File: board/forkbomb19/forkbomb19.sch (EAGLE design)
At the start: 65 parts, among them SW1 SPST_TACT-KMR2, T3 MMUN2133LT1G, U1 ESP-WROOM-03, U4 TPS61090RSAR, U5 MCP73871, X3 POT_GND, X4 POT_3V3, X5 POT_SIG

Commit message: small cleanup
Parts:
- removed HRDRST: JUMPER-SMT_2_NO_SILK_ROUND, SparkFun-Jumpers:JUMPER-SMT_2_NO_SILK_ROUND
- added SW2: SPST_TACT-KMR2, adafruit:SPST_TACT-KMR2
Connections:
- net EN: now also SW2.S, SW2.S1; no longer HRDRST.2
- net GND: now also SW2.P, SW2.P1; no longer HRDRST.1
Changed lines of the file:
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@@
 <parts>
 <part name="U1" library="forkbomb19" deviceset="ESP-WROOM-03" device=""/>
-<part name="HRDRST" library="SparkFun-Jumpers" library_urn="urn:adsk.eagle:library:528" deviceset="JUMPER-SMT_2_NO" device="_SILK_ROUND" package3d_urn="urn:adsk.eagle:package:39280/1" value=""/>
 <part name="R1" library="resistor" library_urn="urn:adsk.eagle:library:348" deviceset="R-US_" device="R0603" package3d_urn="urn:adsk.eagle:package:23555/2" value="1k"/>
 <part name="C1" library="resistor" library_urn="urn:adsk.eagle:library:348" deviceset="C-US" device="C0603" package3d_urn="urn:adsk.eagle:package:23616/2" value="100nF"/>
@@
 <part name="U$20" library="microbuilder" deviceset="GND" device=""/>
 <part name="U$23" library="microbuilder" deviceset="VBAT" device=""/>
-<part name="T3" library="transistor" deviceset="*-PNP_DRIVER-" device="SC59-BEC" technology="MUN2114T1" value="MMUN2133LT1G"/>
+<part name="T3" library="transistor" library_urn="urn:adsk.eagle:library:402" deviceset="*-PNP_DRIVER-" device="SC59-BEC" package3d_urn="urn:adsk.eagle:package:28754/2" technology="MUN2114T1" value="MMUN2133LT1G"/>
 <part name="GND22" library="supply1" deviceset="GND" device=""/>
 <part name="R25" library="rcl" library_urn="urn:adsk.eagle:library:334" deviceset="R-US_" device="R0603" package3d_urn="urn:adsk.eagle:package:23555/2" value="270K"/>
@@
 <part name="+3V16" library="supply1" library_urn="urn:adsk.eagle:library:371" deviceset="+3V3" device=""/>
 <part name="U$8" library="forkbomb19" deviceset="JS202011JAQN" device=""/>
+<part name="SW2" library="adafruit" library_urn="urn:adsk.eagle:library:420" deviceset="SPST_TACT" device="-KMR2" package3d_urn="urn:adsk.eagle:package:6240885/1"/>
 </parts>
 <sheets>
@@
 <attribute name="VALUE" x="-15.24" y="-38.354" size="1.778" layer="96" align="top-left"/>
 </instance>
-<instance part="HRDRST" gate="G$1" x="-35.56" y="30.48" smashed="yes">
-<attribute name="NAME" x="-38.1" y="33.02" size="1.778" layer="95" font="vector"/>
-<attribute name="VALUE" x="-38.1" y="27.94" size="1.778" layer="96" font="vector" align="top-left"/>
-</instance>
 <instance part="R1" gate="G$1" x="-25.4" y="35.56" smashed="yes" rot="R90">
 <attribute name="NAME" x="-26.8986" y="31.75" size="1.778" layer="95" rot="R90"/>
@@
 <attribute name="VALUE" x="-20.32" y="45.72" size="1.778" layer="96" rot="R90"/>
 </instance>
-<instance part="GND2" gate="1" x="-43.18" y="25.4" smashed="yes">
-<attribute name="VALUE" x="-45.72" y="22.86" size="1.778" layer="96"/>
+<instance part="GND2" gate="1" x="-48.26" y="25.4" smashed="yes">
+<attribute name="VALUE" x="-50.8" y="22.86" size="1.778" layer="96"/>
 </instance>
 <instance part="GND3" gate="1" x="-2.54" y="40.64" smashed="yes">
@@
 </instance>
 <instance part="+3V2" gate="G$1" x="66.04" y="-25.4" smashed="yes">
-<attribute name="VALUE" x="63.5" y="-30.48" size="1.778" layer="96" rot="R90"/>
+<attribute name="VALUE" x="68.58" y="-25.4" size="1.778" layer="96"/>
 </instance>
 <instance part="C3" gate="G$1" x="25.4" y="48.26" smashed="yes">
@@
 </instance>
 <instance part="X3" gate="-1" x="66.04" y="-44.45" smashed="yes" rot="R90">
-<attribute name="VALUE" x="64.77" y="-45.72" size="1.778" layer="96" rot="R90"/>
-<attribute name="NAME" x="66.802" y="-41.91" size="1.524" layer="95" rot="R90"/>
+<attribute name="VALUE" x="63.5" y="-57.15" size="1.778" layer="96"/>
+<attribute name="NAME" x="72.39" y="-54.102" size="1.524" layer="95"/>
 </instance>
 <instance part="X4" gate="-1" x="66.04" y="-31.75" smashed="yes" rot="R270">
-<attribute name="VALUE" x="67.31" y="-30.48" size="1.778" layer="96" rot="R270"/>
-<attribute name="NAME" x="65.278" y="-34.29" size="1.524" layer="95" rot="R270"/>
+<attribute name="VALUE" x="68.58" y="-29.21" size="1.778" layer="96"/>
+<attribute name="NAME" x="69.85" y="-31.242" size="1.524" layer="95"/>
 </instance>
 <instance part="X5" gate="-1" x="62.23" y="-38.1" smashed="yes">
-<attribute name="VALUE" x="60.96" y="-36.83" size="1.778" layer="96"/>
-<attribute name="NAME" x="64.77" y="-38.862" size="1.524" layer="95"/>
+<attribute name="VALUE" x="48.26" y="-41.91" size="1.778" layer="96"/>
+<attribute name="NAME" x="59.69" y="-41.402" size="1.524" layer="95"/>
 </instance>
 <instance part="SW1" gate="G$1" x="43.18" y="-25.4" smashed="yes" rot="R270">
@@
 </instance>
 <instance part="U$8" gate="G$1" x="-162.56" y="86.36" smashed="yes"/>
+<instance part="SW2" gate="G$1" x="-40.64" y="33.02" smashed="yes" rot="R270">
+<attribute name="NAME" x="-43.18" y="39.37" size="1.778" layer="95"/>
+<attribute name="VALUE" x="-37.465" y="36.83" size="1.778" layer="96"/>
+</instance>
 </instances>
 <busses>
@@
 <pinref part="R1" gate="G$1" pin="1"/>
 <wire x1="-17.78" y1="30.48" x2="-25.4" y2="30.48" width="0.1524" layer="91"/>
-<pinref part="HRDRST" gate="G$1" pin="2"/>
-<wire x1="-25.4" y1="30.48" x2="-30.48" y2="30.48" width="0.1524" layer="91"/>
+<wire x1="-25.4" y1="30.48" x2="-35.56" y2="30.48" width="0.1524" layer="91"/>
 <junction x="-25.4" y="30.48"/>
 <label x="-17.78" y="30.48" size="1.778" layer="95" rot="R180"/>
+<pinref part="SW2" gate="G$1" pin="S1"/>
+<pinref part="SW2" gate="G$1" pin="S"/>
+<wire x1="-35.56" y1="33.02" x2="-35.56" y2="30.48" width="0.1524" layer="91"/>
+<junction x="-35.56" y="30.48"/>
 </segment>
 <segment>
@@
 <segment>
 <pinref part="GND2" gate="1" pin="GND"/>
-<pinref part="HRDRST" gate="G$1" pin="1"/>
-<wire x1="-43.18" y1="27.94" x2="-43.18" y2="30.48" width="0.1524" layer="91"/>
-<wire x1="-43.18" y1="30.48" x2="-40.64" y2="30.48" width="0.1524" layer="91"/>
-</segment>
-<segment>
+<wire x1="-48.26" y1="27.94" x2="-48.26" y2="30.48" width="0.1524" layer="91"/>
+<wire x1="-48.26" y1="30.48" x2="-45.72" y2="30.48" width="0.1524" layer="91"/>
+<pinref part="SW2" gate="G$1" pin="P1"/>
+<pinref part="SW2" gate="G$1" pin="P"/>
+<wire x1="-45.72" y1="33.02" x2="-45.72" y2="30.48" width="0.1524" layer="91"/>
+<junction x="-45.72" y="30.48"/>
+</segment>
+<segment>

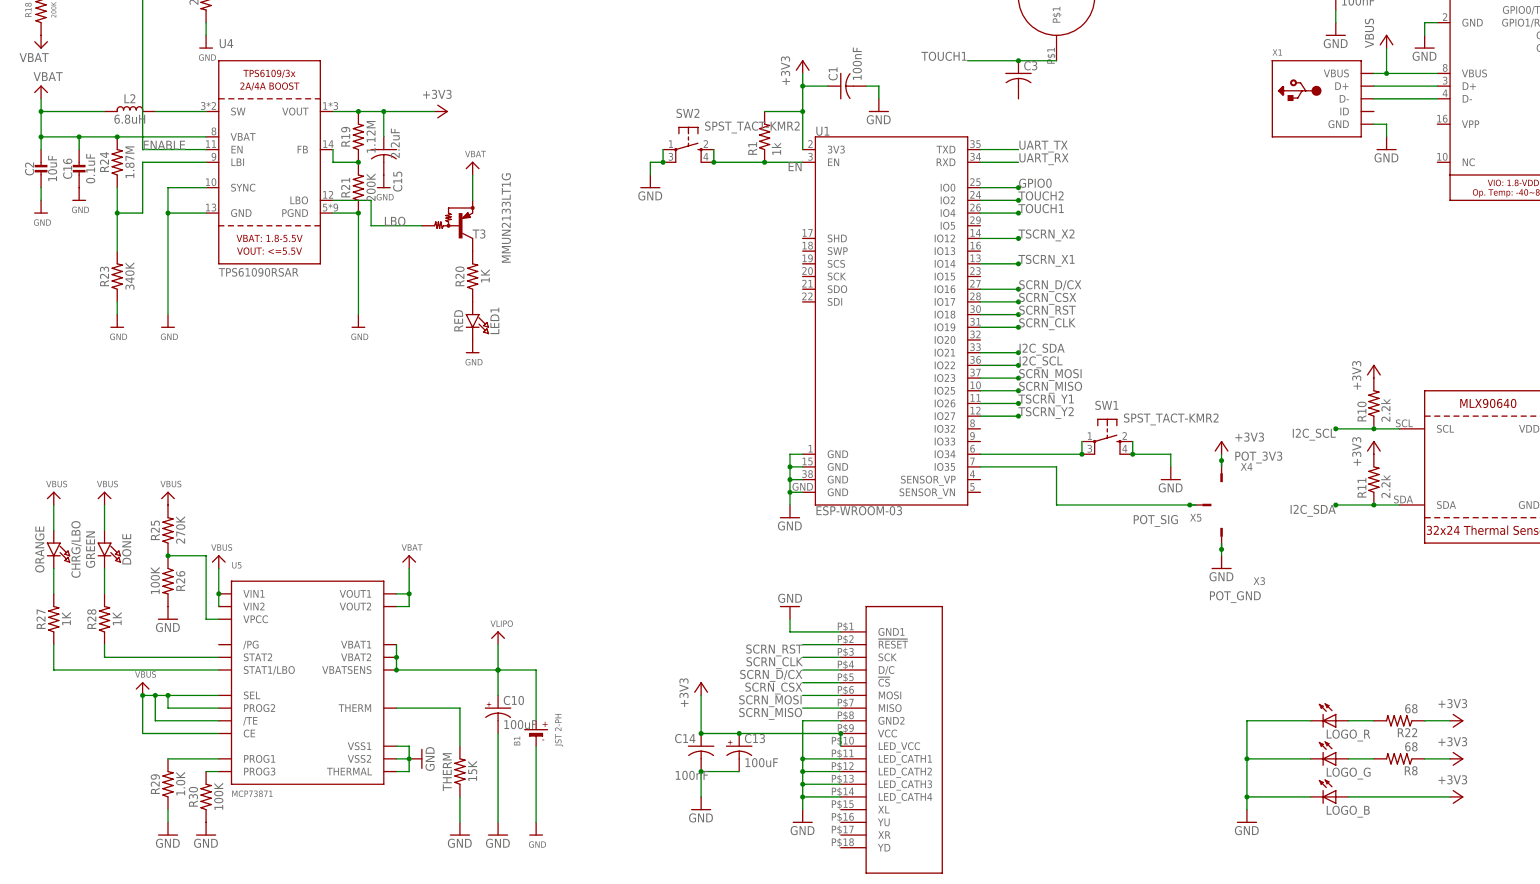
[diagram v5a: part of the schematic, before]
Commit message: made a BOM, cleaned up the board, added a styles 27 button
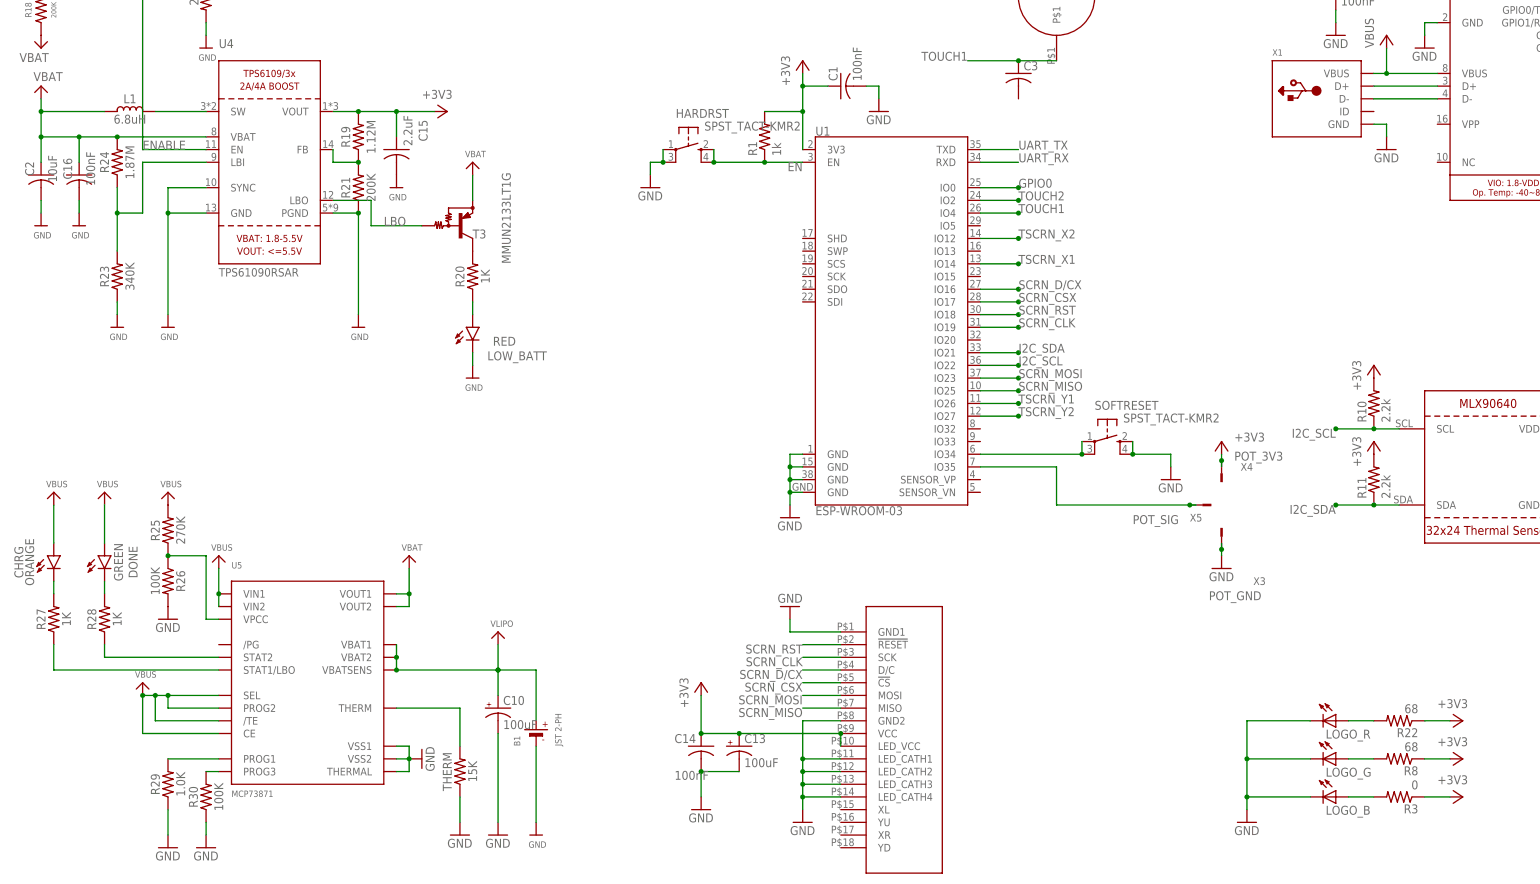
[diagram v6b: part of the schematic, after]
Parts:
- removed CHRG/LBO: ORANGE, microbuilder:LED0805_NOOUTLINE
- removed LED1: RED, microbuilder:LED0805_NOOUTLINE
- added CHRG: ORANGE, led:LEDCHIP-LED0603
- added LOW_BATT: RED, led:LEDCHIP-LED0603
- added R3: 0, resistor:R-US_R0805
- C16: value 0.1uF -> 100nF; device microbuilder:CAP_CERAMIC0805_10MGAP -> rcl:C-USC0603
- C2: device microbuilder:CAP_CERAMIC0805-NOOUTLINE -> rcl:C-USC1210
- DONE: device microbuilder:LED0805_NOOUTLINE -> led:LEDCHIP-LED0603
- RX, TX: device led:LEDSML0603 -> led:LEDCHIP-LED0603
- T1, T2: device transistor-neu-to92:MMBT2222ALT1-NPN-SOT23-BEC -> transistor:MMBT3904LT1-NPN-SOT23-BEC
- renumbered L2 to L1, SW1 to SOFTRESET, SW2 to HARDRST
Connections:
- new net N$7: LOGO_B.A, R3.2
- net +3V3: now also R3.1; no longer LOGO_B.A
- net GND: now also LOW_BATT.C; no longer LED1.C
- net N$24: now also LOW_BATT.A; no longer LED1.A
- net N$36: now also CHRG.C; no longer CHRG/LBO.C
- net VBUS: now also CHRG.A; no longer CHRG/LBO.A
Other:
- moved on the sheet: C15, C16, C2

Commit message: cleaning up board and schematic
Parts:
- removed C3: (no value), resistor:C-USC0805
- added FRAME1: FRAME-LEDGER, SparkFun-Aesthetics:FRAME-LEDGER
- added LOGO1: OSHW-LOGOS-COPPER, SparkFun-Aesthetics:OSHW-LOGOS-COPPER
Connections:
- net TOUCH1: no longer C3.1, TOUCH.P$1
- net TOUCH2: now also TOUCH.P$1
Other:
- note added: "1.0"
- note added: "6/9/19"
- note added: "Control/Indication"
- note added: "ESP32-WROOM-32"
- note added: "Forkbomb Defcon 27 Badge"
- note added: "Grant Haack"
- note added: "Power Management"
- note added: "TFT LCD"
- note added: "Thermal Sensor"
- note added: "USB-UART Bridge"
- moved on the sheet: B1, C1, C10, C11, C12, C13, C14, C9, CHRG, DONE, HARDRST, LOGO_B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
